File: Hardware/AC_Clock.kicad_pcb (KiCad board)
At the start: 2 copper layers, 132.1 x 100.3 mm, 72 parts, among them J1 L, J2 N, J3 Conn_01x10, J4 Conn_01x10, J5 Conn_01x10, J6 Conn_01x10, SW1 Min_PB, SW2 Hr_PB, T1 10:1, U1 AZ1117-5.0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

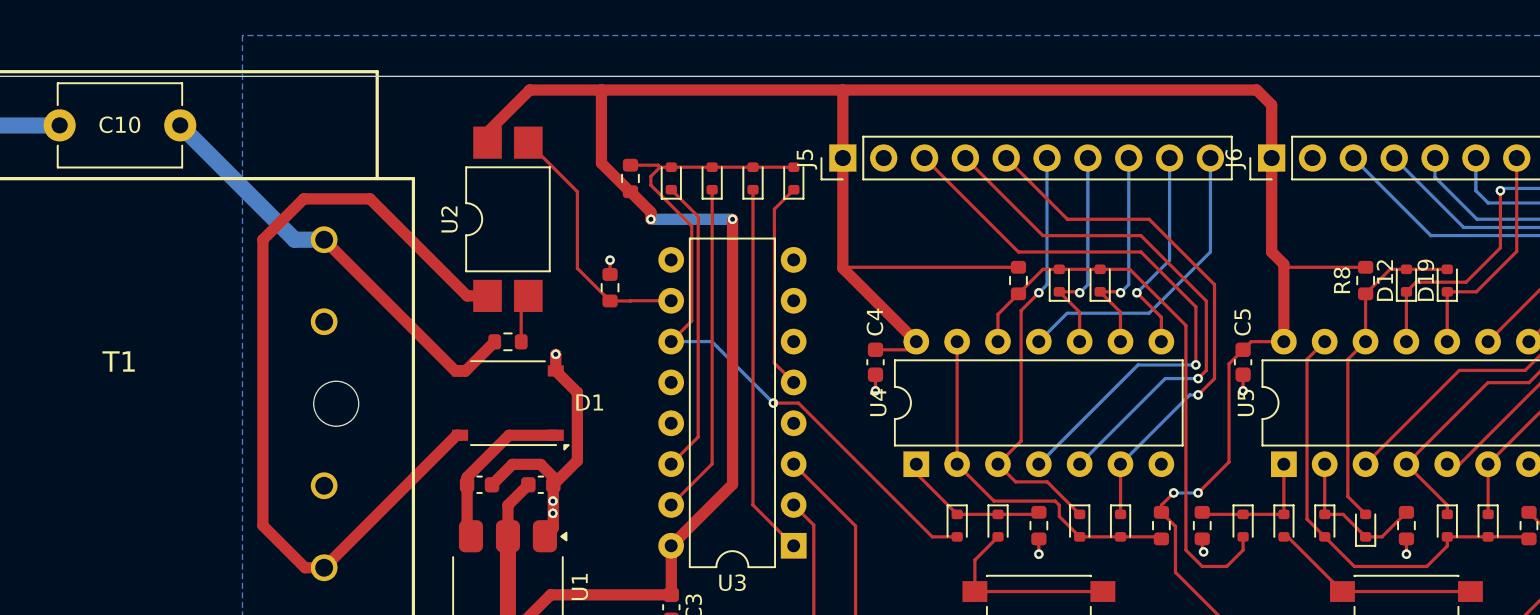
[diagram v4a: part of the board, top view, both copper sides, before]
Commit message: Fix routing and clean up silkscreen
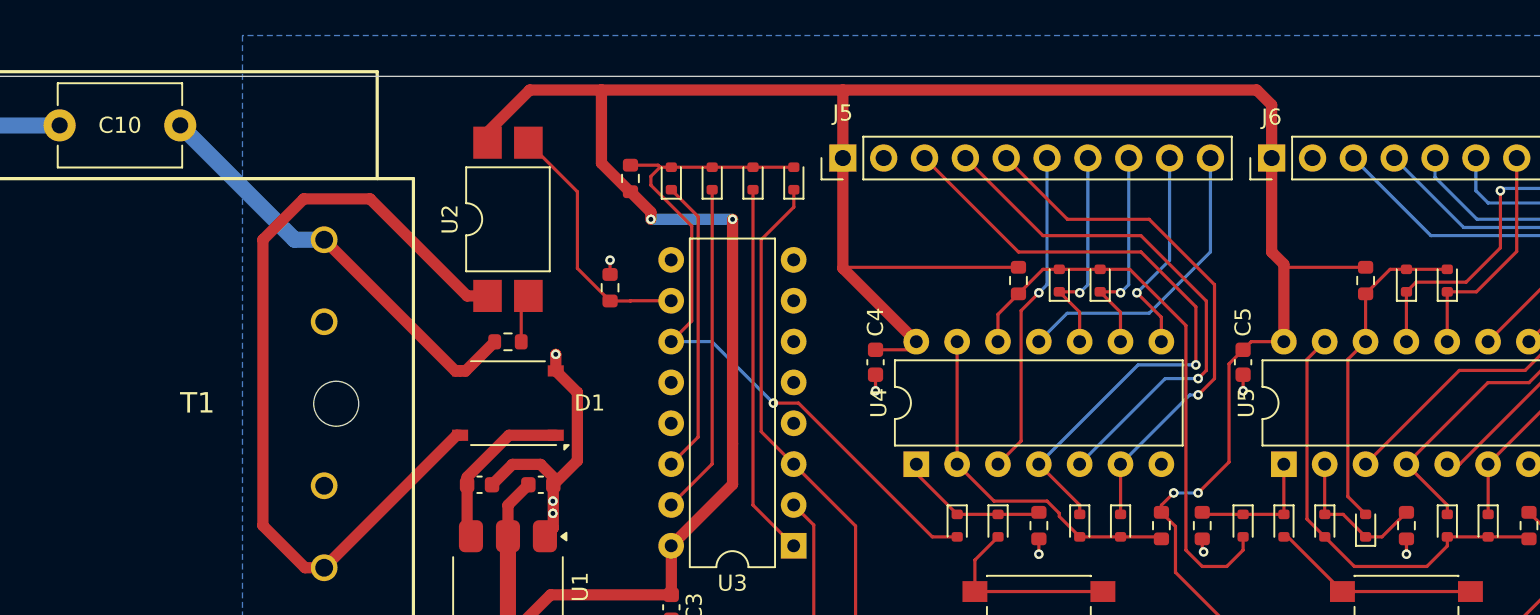
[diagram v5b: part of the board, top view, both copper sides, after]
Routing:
- net /2Hz: track 13.0 -> 31.8 mm
- net /4Hz: track 13.0 -> 0.00 mm
- net DA_1: track 39.6 -> 33.3 mm
- net DB_1: track 48.1 -> 52.2 mm
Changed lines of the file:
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@@
 		(tags "Transformer 12VAC 5VA")
 		(property "Reference" "T1"
-			(at 0 -2.54 180)
+			(at 4.826 0 180)
 			(layer "F.SilkS")
 			(effects
@@
 		(tags "Through hole pin header THT 1x10 2.54mm single row")
 		(property "Reference" "J6"
-			(at 0 -2.33 90)
+			(at 2.54 0 180)
 			(layer "F.SilkS")
 			(effects
@@
 			(at 0 -1.3 90)
 			(layer "F.SilkS")
+			(hide yes)
 			(effects
 				(font
@@
 			(at 0 -1.43 90)
 			(layer "F.SilkS")
+			(hide yes)
 			(effects
 				(font
@@
 			(at 0 -1.3 90)
 			(layer "F.SilkS")
+			(hide yes)
 			(effects
 				(font
@@
 		(tags "Through hole pin header THT 1x10 2.54mm single row")
 		(property "Reference" "J5"
-			(at 0 -2.33 90)
+			(at 2.794 0 180)
 			(layer "F.SilkS")
 			(effects
@@
 	)
 	(segment
-		(start 104.2 124.515)
-		(end 104.2 114.94)
-		(width 0.2)
-		(layer "F.Cu")
-		(net 7)
-	)
-	(segment
-		(start 104.2 114.94)
-		(end 105.41 113.73)
-		(width 0.2)
-		(layer "F.Cu")
-		(net 7)
-	)
-	(segment
-		(start 105.4 125.715)
-		(end 104.2 124.515)
-		(width 0.2)
-		(layer "F.Cu")
-		(net 7)
-	)
-	(segment
 		(start 90.891 74.381)
 		(end 96.52 80.01)
@@
 	)
 	(segment
-		(start 121.92 134.05)
-		(end 121.92 133.35)
+		(start 128.27 135.445)
+		(end 128.145 135.32)
 		(width 0.2)
 		(layer "F.Cu")
@@
 	)
 	(segment
-		(start 128.27 135.445)
-		(end 128.145 135.32)
+		(start 121.92 134.05)
+		(end 121.92 133.858)
 		(width 0.2)
 		(layer "F.Cu")
@@
 	)
 	(segment
-		(start 117.86 133.095)
-		(end 115.565 130.8)
+		(start 121.157 133.095)
+		(end 117.86 133.095)
 		(width 0.2)
 		(layer "F.Cu")
@@
 	)
 	(segment
-		(start 121.665 133.095)
-		(end 117.86 133.095)
+		(start 123.19 135.32)
+		(end 121.92 134.05)
 		(width 0.2)
 		(layer "F.Cu")
@@
 	)
 	(segment
-		(start 123.19 135.32)
-		(end 121.92 134.05)
+		(start 117.86 133.095)
+		(end 115.565 130.8)
 		(width 0.2)
 		(layer "F.Cu")
@@
 	)
 	(segment
-		(start 121.92 133.35)
-		(end 121.665 133.095)
+		(start 121.92 133.858)
+		(end 121.157 133.095)
 		(width 0.2)
 		(layer "F.Cu")
@@
 	)
 	(segment
-		(start 119.205 131.9)
-		(end 121.17 131.9)
-		(width 0.2)
-		(layer "F.Cu")
-		(net 10)
-	)
-	(segment
 		(start 119.545 121.247)
 		(end 120.65 120.142)
@@
 		(net 10)
 	)
-	(segment
-		(start 121.17 131.9)
-		(end 123.19 133.92)
-		(width 0.2)
-		(layer "F.Cu")
-		(net 10)
-	)
-	(segment
-		(start 118.105 130.8)
-		(end 119.205 131.9)
-		(width 0.2)
-		(layer "F.Cu")
-		(net 10)
-	)
 	(via
 		(at 120.65 120.142)
@@
 	)
 	(segment
+		(start 105.41 114.808)
+		(end 105.41 113.73)
+		(width 0.2)
+		(layer "F.Cu")
+		(net 26)
+	)
+	(segment
+		(start 103.378 116.84)
+		(end 105.41 114.808)
+		(width 0.2)
+		(layer "F.Cu")
+		(net 26)
+	)
+	(segment
+		(start 103.378 128.773)
+		(end 103.378 116.84)
+		(width 0.2)
+		(layer "F.Cu")
+		(net 26)
+	)
+	(segment
 		(start 109.25 134.645)
 		(end 109.25 142.24)
@@
 	(segment
 		(start 105.4 130.795)
+		(end 103.378 128.773)
+		(width 0.2)
+		(layer "F.Cu")
+		(net 26)
+	)
+	(segment
+		(start 105.4 130.795)
 		(end 109.25 134.645)
 		(width 0.2)
@@
 	)
 	(segment
+		(start 123.19 133.345)
+		(end 123.19 133.92)
+		(width 0.2)
+		(layer "F.Cu")
+		(net 50)
+	)
+	(segment
 		(start 119.38 117.602)
 		(end 127 117.602)
@@
 		(width 0.2)
 		(layer "F.Cu")
+		(net 50)
+	)
+	(segment
+		(start 120.645 130.8)
+		(end 123.19 133.345)
+		(width 0.2)
+		(layer "F.Cu")

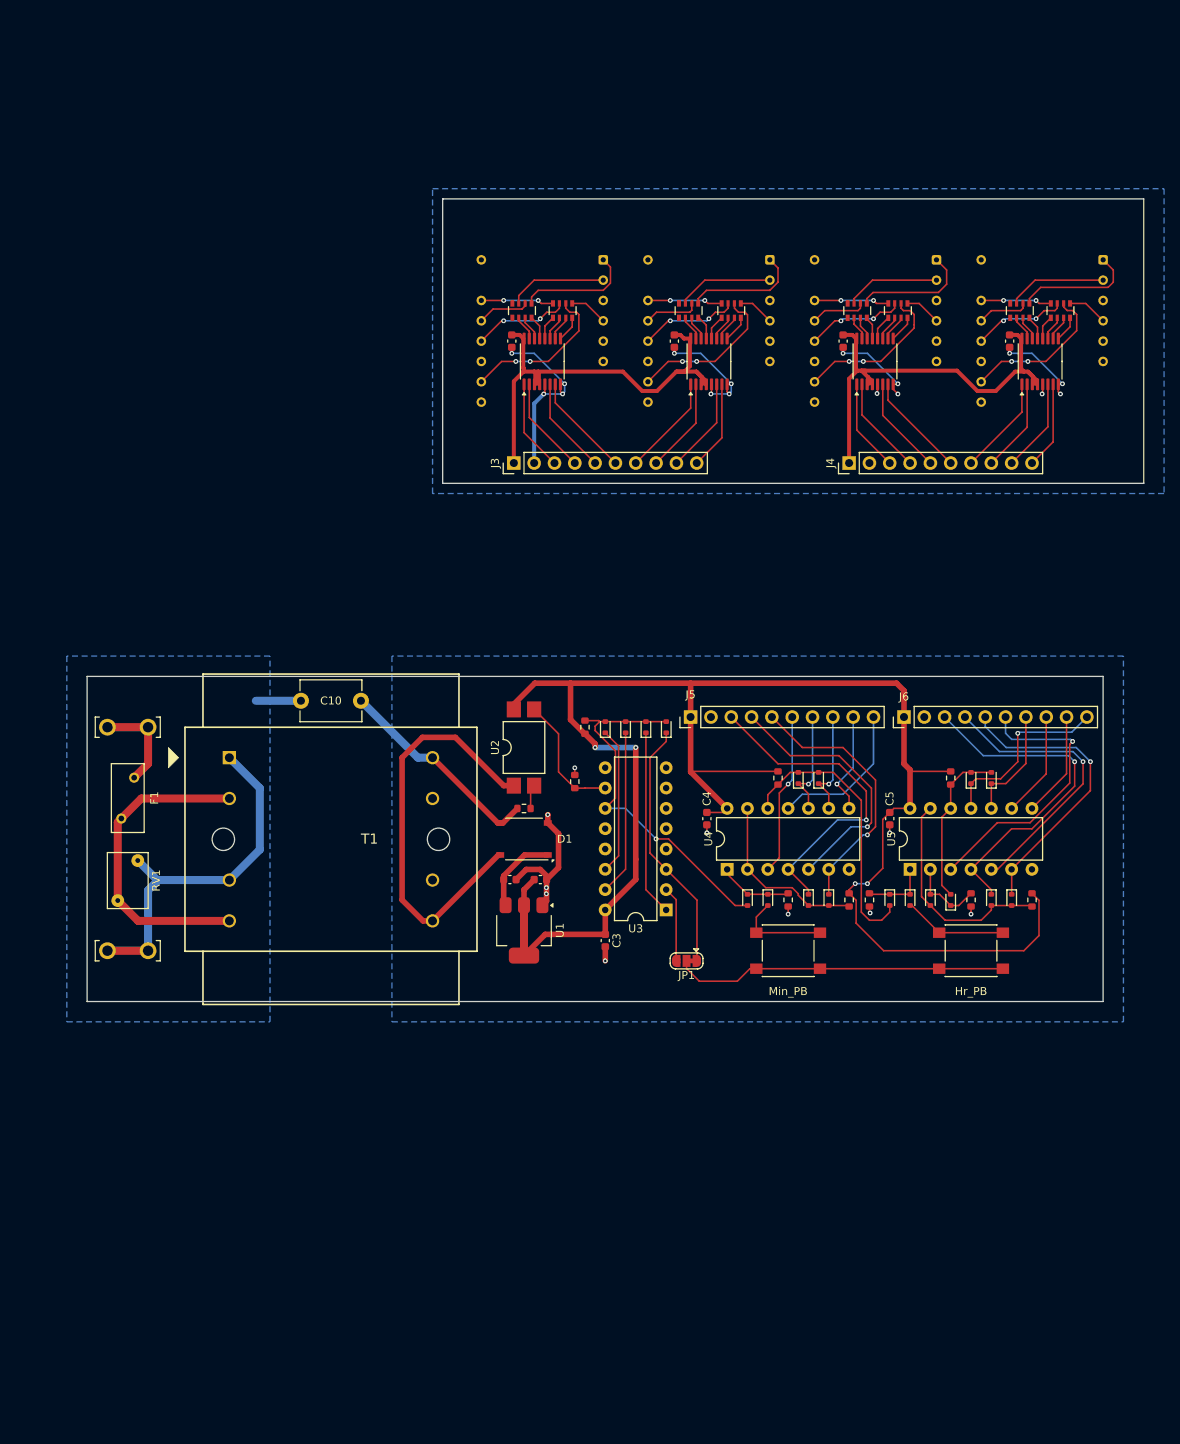
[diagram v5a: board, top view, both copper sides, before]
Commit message: Convert layout to 3 board design (power/logic/display)
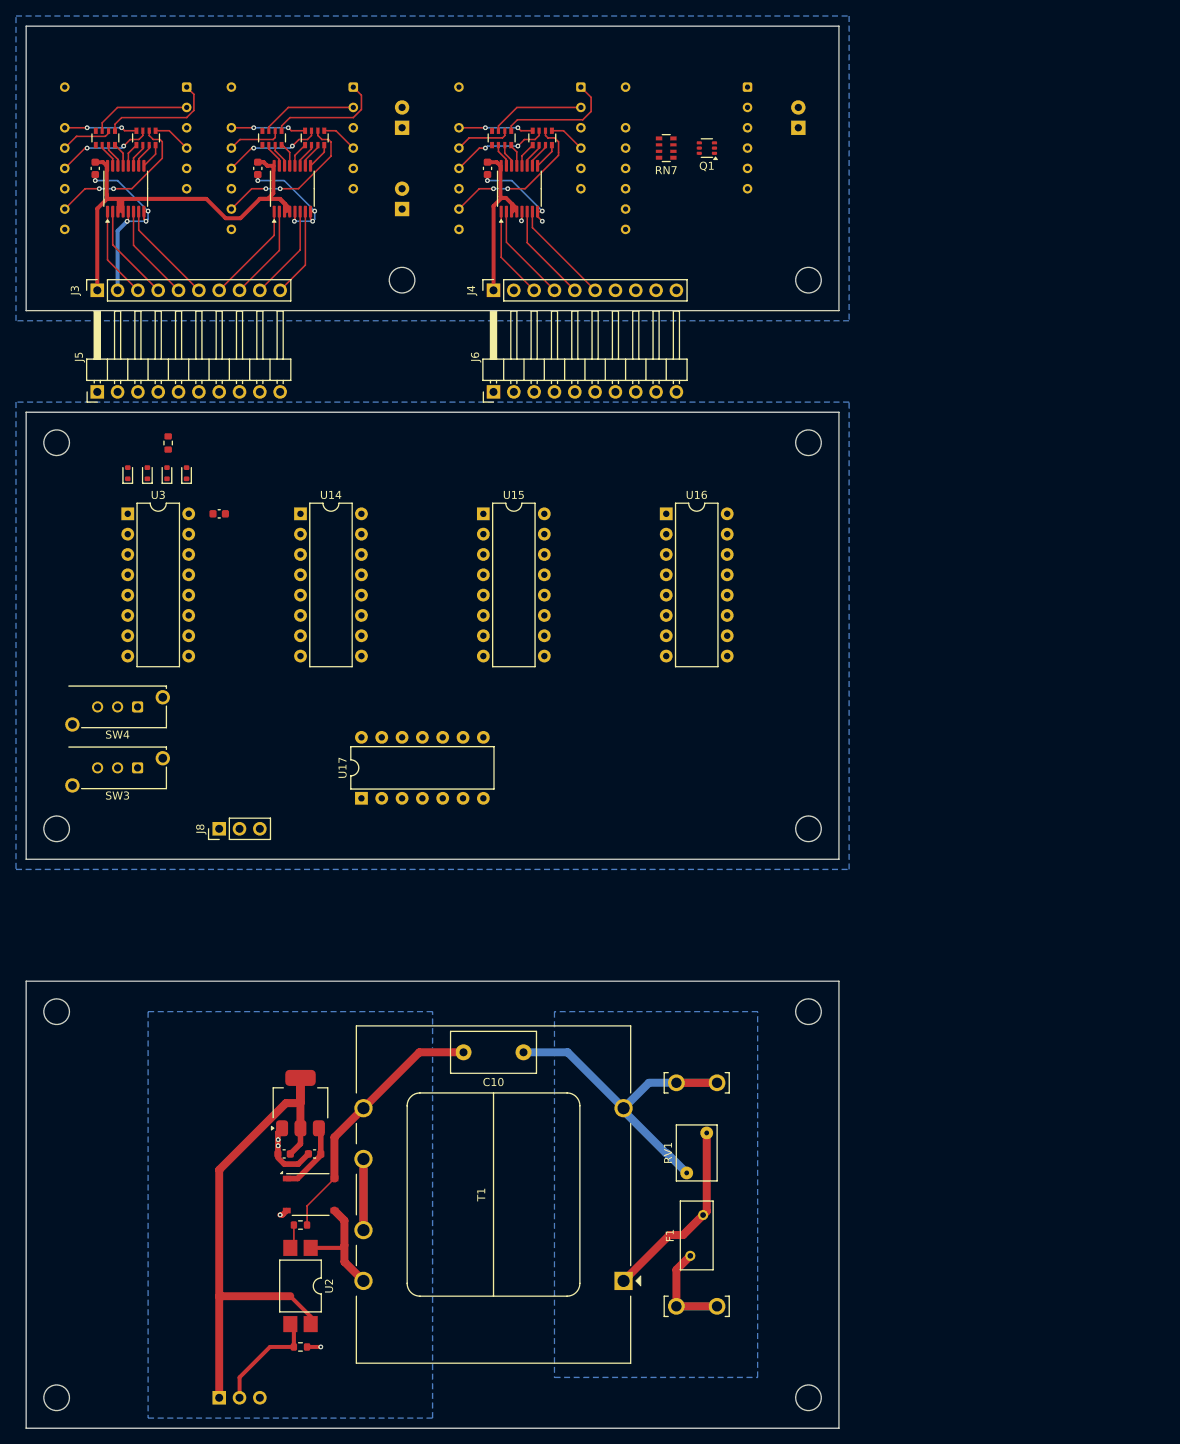
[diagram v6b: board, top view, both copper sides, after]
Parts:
- removed C4, C5, C9: 0.1u, Capacitor_SMD:C_0603_1608Metric
- removed D10, D11, D12, D13, D14, D15, D16, D17, D18, D19, D6, D7, D8, D9: 1N4148WT, Diode_SMD:D_SOD-523
- removed JP1: Freq Sel., Jumper:SolderJumper-3_P1.3mm_Bridged12_RoundedPad1.0x1.5mm
- removed R10, R4, R5, R6, R7, R8, R9: 1k, Resistor_SMD:R_0603_1608Metric
- removed RN8: 1k, Resistor_SMD:R_Array_Convex_4x0603
- removed SW1: Min_PB, Button_Switch_SMD:SW_SPST_PTS645
- removed SW2: Hr_PB, Button_Switch_SMD:SW_SPST_PTS645
- removed U12: 4511, Package_SO:TSSOP-16_4.4x5mm_P0.65mm
- removed U4, U5: 74LS393, Package_DIP:DIP-14_W7.62mm
- added D20: PM, LED_THT:LED_D5.0mm, B.Cu at (121.9, 38.1)
- added J7: PWR, Connector_PinSocket_2.54mm:PinSocket_1x03_P2.54mm_Vertical, B.Cu at (49.5, 196.8)
- added J8: PWR, Connector_PinHeader_2.54mm:PinHeader_1x03_P2.54mm_Vertical, F.Cu at (49.5, 125.7)
- added Q1: BSS138, Package_TO_SOT_SMD:SOT-363_SC-70-6, F.Cu at (110.5, 40.6)
- added REF**: MountingHole_3.2mm_M3, MountingHole:MountingHole_3.2mm_M3, F.Cu at (72.4, 57.1)
- added REF**: MountingHole_3.2mm_M3, MountingHole:MountingHole_3.2mm_M3, F.Cu at (123.2, 196.8)
- added REF**: LED_D5.0mm, LED_THT:LED_D5.0mm, B.Cu at (72.4, 48.3)
- added REF**: LED_D5.0mm, LED_THT:LED_D5.0mm, B.Cu at (72.4, 38.1)
- added REF**: MountingHole_3.2mm_M3, MountingHole:MountingHole_3.2mm_M3, F.Cu at (123.2, 148.6)
- added REF**: MountingHole_3.2mm_M3, MountingHole:MountingHole_3.2mm_M3, F.Cu at (29.2, 77.5)
- added REF**: MountingHole_3.2mm_M3, MountingHole:MountingHole_3.2mm_M3, F.Cu at (29.2, 148.6)
- added REF**: MountingHole_3.2mm_M3, MountingHole:MountingHole_3.2mm_M3, F.Cu at (123.2, 77.5)
- added REF**: MountingHole_3.2mm_M3, MountingHole:MountingHole_3.2mm_M3, F.Cu at (29.2, 125.7)
- added REF**: MountingHole_3.2mm_M3, MountingHole:MountingHole_3.2mm_M3, F.Cu at (123.2, 125.7)
- added REF**: MountingHole_3.2mm_M3, MountingHole:MountingHole_3.2mm_M3, F.Cu at (29.2, 196.8)
- added REF**: MountingHole_3.2mm_M3, MountingHole:MountingHole_3.2mm_M3, F.Cu at (123.2, 57.1)
- added SW3: Hour Set, JKC_Library:SW_Push_CK_PN11SBNA03QE_SPDT_Right_Angle, F.Cu at (36.8, 118.1)
- added SW4: Min Set, JKC_Library:SW_Push_CK_PN11SBNA03QE_SPDT_Right_Angle, F.Cu at (36.8, 110.5)
- added U14: 4518, Package_DIP:DIP-16_W7.62mm, F.Cu at (59.7, 86.4)
- added U15: 4510, Package_DIP:DIP-16_W7.62mm, F.Cu at (82.5, 86.4)
- added U16: 4027, Package_DIP:DIP-16_W7.62mm, F.Cu at (105.4, 86.4)
- added U17: 4081, Package_DIP:DIP-14_W7.62mm, F.Cu at (67.3, 121.9)
- C10: footprint Capacitor_THT:C_Disc_D7.5mm_W5.0mm_P7.50mm -> Capacitor_THT:C_Disc_D10.5mm_W5.0mm_P7.50mm
- J3, J4: footprint Connector_PinHeader_2.54mm:PinHeader_1x10_P2.54mm_Vertical -> Connector_PinSocket_2.54mm:PinSocket_1x10_P2.54mm_Vertical
- J5: value Conn_01x10 -> Minutes; footprint Connector_PinHeader_2.54mm:PinHeader_1x10_P2.54mm_Vertical -> Connector_PinHeader_2.54mm:PinHeader_1x10_P2.54mm_Horizontal
- J6: value Conn_01x10 -> Hours; footprint Connector_PinHeader_2.54mm:PinHeader_1x10_P2.54mm_Vertical -> Connector_PinHeader_2.54mm:PinHeader_1x10_P2.54mm_Horizontal
- T1: value 10:1 -> F12-500-C2; footprint JKC_Library:Transformer_CL2-5.0R-12 -> JKC_Library:XFMR_Triad_F12-500-C2
- moved J1 101.5 mm to (109.2, 185.4), turned to 180 degrees
- moved F1 91.7 mm to (108.4, 179.1), turned to 90 degrees
- moved J5 84.6 mm to (34.3, 71.1)
- moved U3 83.6 mm to (38.1, 86.4), turned to 0 degrees
- moved RV1 79.1 mm to (110.5, 163.8), turned to -90 degrees
- moved R2 78.6 mm to (59.7, 190.5), turned to 0 degrees
- moved J2 73.0 mm to (109.2, 157.5), turned to 180 degrees
- moved U2 72.9 mm to (59.7, 182.9), turned to -90 degrees
- moved D2 72.1 mm to (38.1, 81.3)
- moved C3 71.9 mm to (49.5, 86.4), turned to 0 degrees
- moved D5 67.8 mm to (45.5, 81.3)
- moved D3 67.7 mm to (40.5, 81.3)
- moved J6 65.5 mm to (83.8, 71.1)
- moved D4 63.3 mm to (43.0, 81.3)
- moved R3 63.1 mm to (43.1, 77.5), turned to 90 degrees
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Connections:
- D1 pad 3: /AC_12- -> /AC_12+
- D1 pad 4: /AC_12+ -> /AC_12-
- J4 pad 10: DA_4 -> unconnected-(J4-Pin_10-Pad10)
- J4 pad 7: DB_4 -> unconnected-(J4-Pin_7-Pad7)
- J4 pad 8: DC_4 -> /Display Driver/10Hr
- J4 pad 9: DD_4 -> /Display Driver/PM
- J6 pad 10: DA_4 -> unconnected-(J6-Pin_10-Pad10)
- J6 pad 7: DB_4 -> unconnected-(J6-Pin_7-Pad7)
- J6 pad 8: DC_4 -> /10Hr
- J6 pad 9: DD_4 -> /PM
- RN7 pad 1: unconnected-(RN7A-R1.1-Pad1) -> Net-(Q1B-S2)
- RN7 pad 2: Net-(RN7B-R2.1) -> Net-(Q1A-S1)
- RN7 pad 3: Net-(RN7C-R3.1) -> Net-(Q1A-S1)
- RN7 pad 4: Net-(RN7D-R4.1) -> unconnected-(RN7D-R4.1-Pad4)
- RN7 pad 5: Net-(RN7D-R4.2) -> unconnected-(RN7D-R4.2-Pad5)
- RN7 pad 8: unconnected-(RN7A-R1.2-Pad8) -> Net-(D20-A)
- T1 pad 1: Earth -> /Fused
- T1 pad 6: /Fused -> Net-(T1-Pad6)
- T1 pad 7: /AC_12- -> Net-(T1-Pad6)
- U13 pad 1: Net-(RN7D-R4.2) -> unconnected-(U13-A-Pad1)
- U13 pad 10: Net-(RN8-R3.2) -> unconnected-(U13-D-Pad10)
- U13 pad 12: Net-(RN8-R2.2) -> Net-(RN7C-R3.2)
- U13 pad 13: Net-(RN7C-R3.2) -> unconnected-(U13-G-Pad13)
- U13 pad 14: Net-(RN8-R1.2) -> Net-(RN7B-R2.2)
- U13 pad 2: Net-(RN7B-R2.2) -> unconnected-(U13-F-Pad2)
- U13 pad 4: Net-(RN8-R4.2) -> unconnected-(U13-E-Pad4)
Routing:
- net +5V: track 324.1 -> 146.2 mm, vias 4 -> 0
- net /minute: track 45.7 -> 0.00 mm, vias 1 -> 0
- net DB_3: track 54.6 -> 11.5 mm, vias 1 -> 0
- net Net-(JP1-C): track 41.8 -> 0.00 mm
- net DB_1: track 52.2 -> 11.4 mm, vias 1 -> 0
- net /AC_12+: track 52.1 -> 14.7 mm
- net DD_3: track 49.1 -> 12.3 mm, vias 1 -> 0
- net DC_3: track 48.1 -> 12.3 mm, vias 1 -> 0
- net DA_3: track 48.6 -> 13.1 mm, vias 1 -> 0
- net /hour: track 35.2 -> 0.00 mm
- net DA_4: track 34.0 -> 0.00 mm, vias 1 -> 0
- net DC_1: track 45.5 -> 12.2 mm, vias 1 -> 0
- net DD_1: track 45.4 -> 12.2 mm, vias 1 -> 0
- net /2Hz: track 31.8 -> 0.00 mm
- net /10hr: track 27.7 -> 0.00 mm
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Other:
- board size 132.1 x 100.3 mm -> 101.6 x 175.3 mm

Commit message: Route traces on new layout
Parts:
- moved J5 8.98 mm to (40.6, 77.5)
- moved R3 6.35 mm to (48.3, 81.3), turned to -90 degrees
- moved J3 6.35 mm to (40.6, 58.4)
- moved J6 6.35 mm to (83.8, 77.5)
- moved D3 5.17 mm to (45.7, 81.3)
- moved D5 4.81 mm to (40.6, 81.3)
- moved D4 0.18 mm to (43.2, 81.3)
- turned Q1 to 0 degrees
- renumbered U14 to U4
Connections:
- net Net-(SW3-B) renamed /hr
- SW4 pad 2: Net-(SW4-B) -> /min
- U4 pad 10: Net-(SW4-B) -> DD_1
- U4 pad 11: DA_1 -> DA_2
- U4 pad 12: DB_1 -> DB_2
- U4 pad 13: DC_1 -> DC_2
- U4 pad 14: DD_1 -> DD_2
- U4 pad 15: GND -> /hour
- U4 pad 2: DD_1 -> /min
- U4 pad 3: DA_2 -> DA_1
- U4 pad 4: DB_2 -> DB_1
- U4 pad 5: DC_2 -> DC_1
- U4 pad 6: DD_2 -> DD_1
- U4 pad 7: /hour -> GND
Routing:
- net +5V: track 146.2 -> 425.3 mm, vias 0 -> 4
- net /hr: track 0.00 -> 80.0 mm, vias 0 -> 3
- net Net-(U15-PE): track 0.00 -> 73.8 mm
- net /hour: track 0.00 -> 73.7 mm, vias 0 -> 3
- net Net-(U16B-C): track 0.00 -> 67.3 mm
- net /10Hr: track 0.00 -> 65.2 mm
- net /2Hz: track 0.00 -> 53.8 mm
- net DB_3: track 11.5 -> 61.0 mm
- net /minute: track 0.00 -> 46.4 mm
- net DA_3: track 13.1 -> 58.1 mm, vias 0 -> 2
- net DD_1: track 12.2 -> 55.2 mm
- net DC_2: track 11.9 -> 54.5 mm, vias 0 -> 1
- net DB_2: track 12.7 -> 54.2 mm, vias 0 -> 1
- net /min: track 0.00 -> 38.2 mm
- net DC_1: track 12.2 -> 45.6 mm
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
